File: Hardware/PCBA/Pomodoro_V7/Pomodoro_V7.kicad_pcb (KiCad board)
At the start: 2 copper layers, 76 x 76 mm, 69 parts, among them IC1 ESP32-S2-MINI-2-N4, J1 Conn_01x02_Socket, J2 Conn_01x01_Pin, J3 Conn_01x01_Pin, J4 USB4120-03-C_REVA

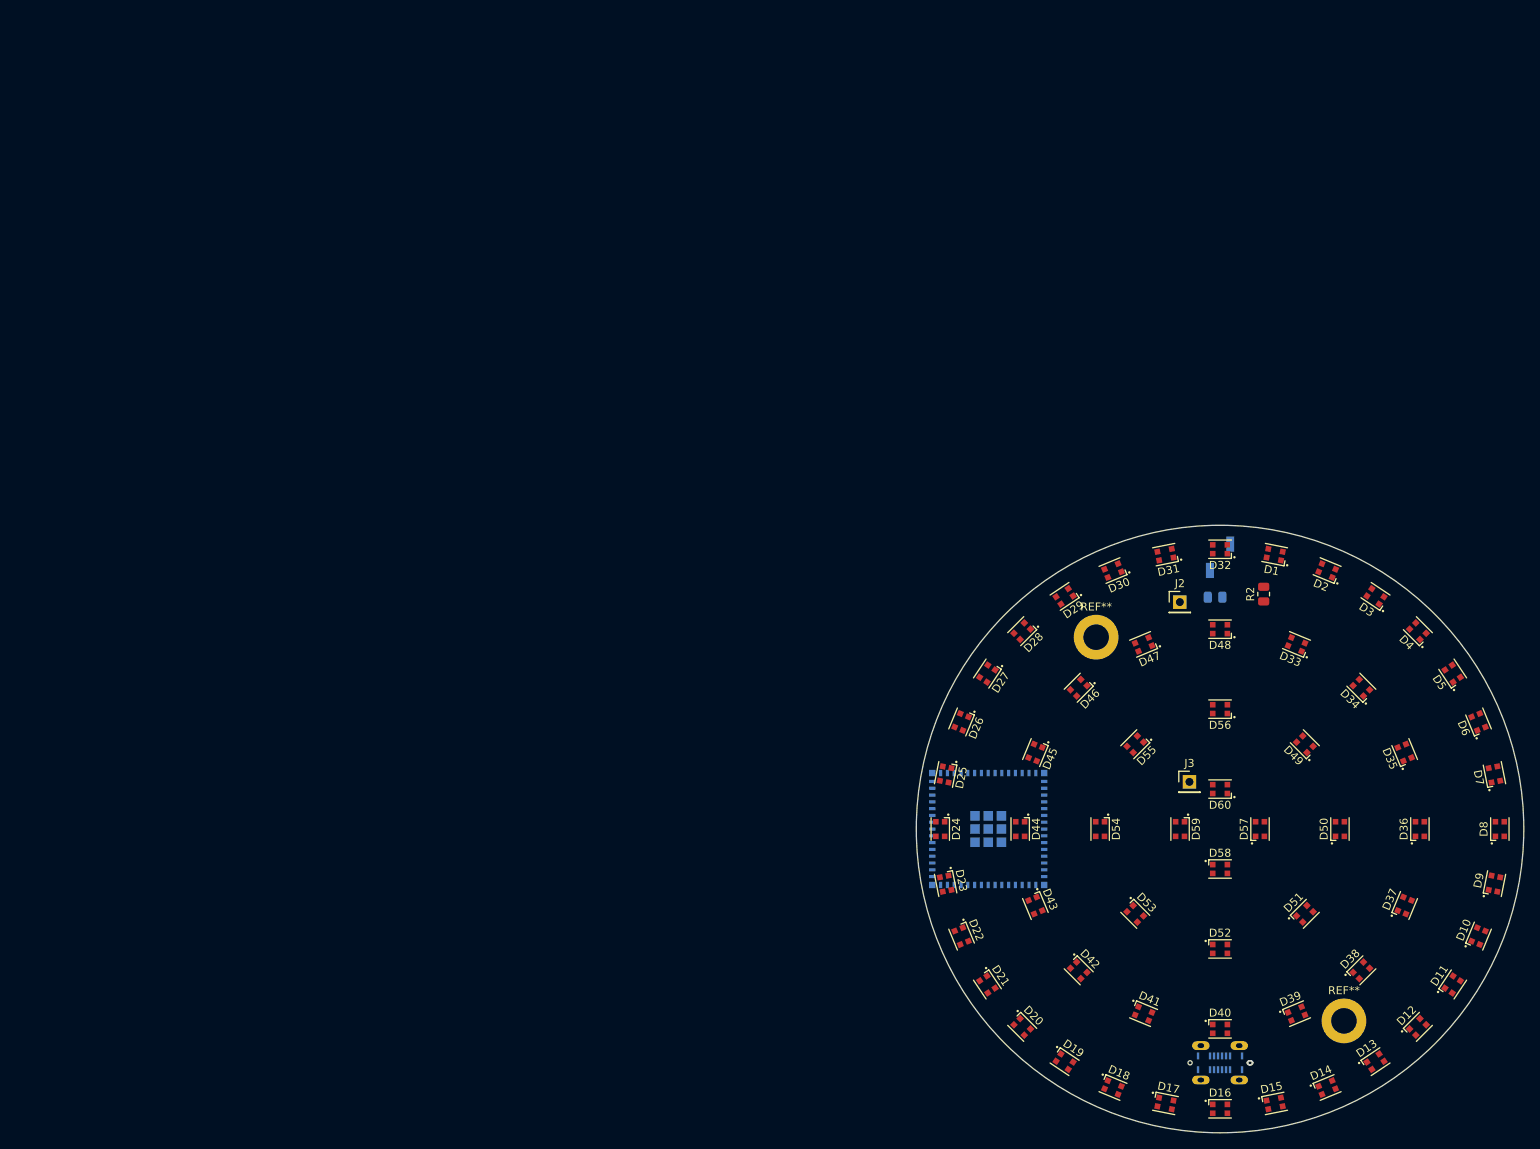
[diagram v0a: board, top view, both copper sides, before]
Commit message: FW can now be flashed to an ESP32-S2 Target; Completed the Schematic
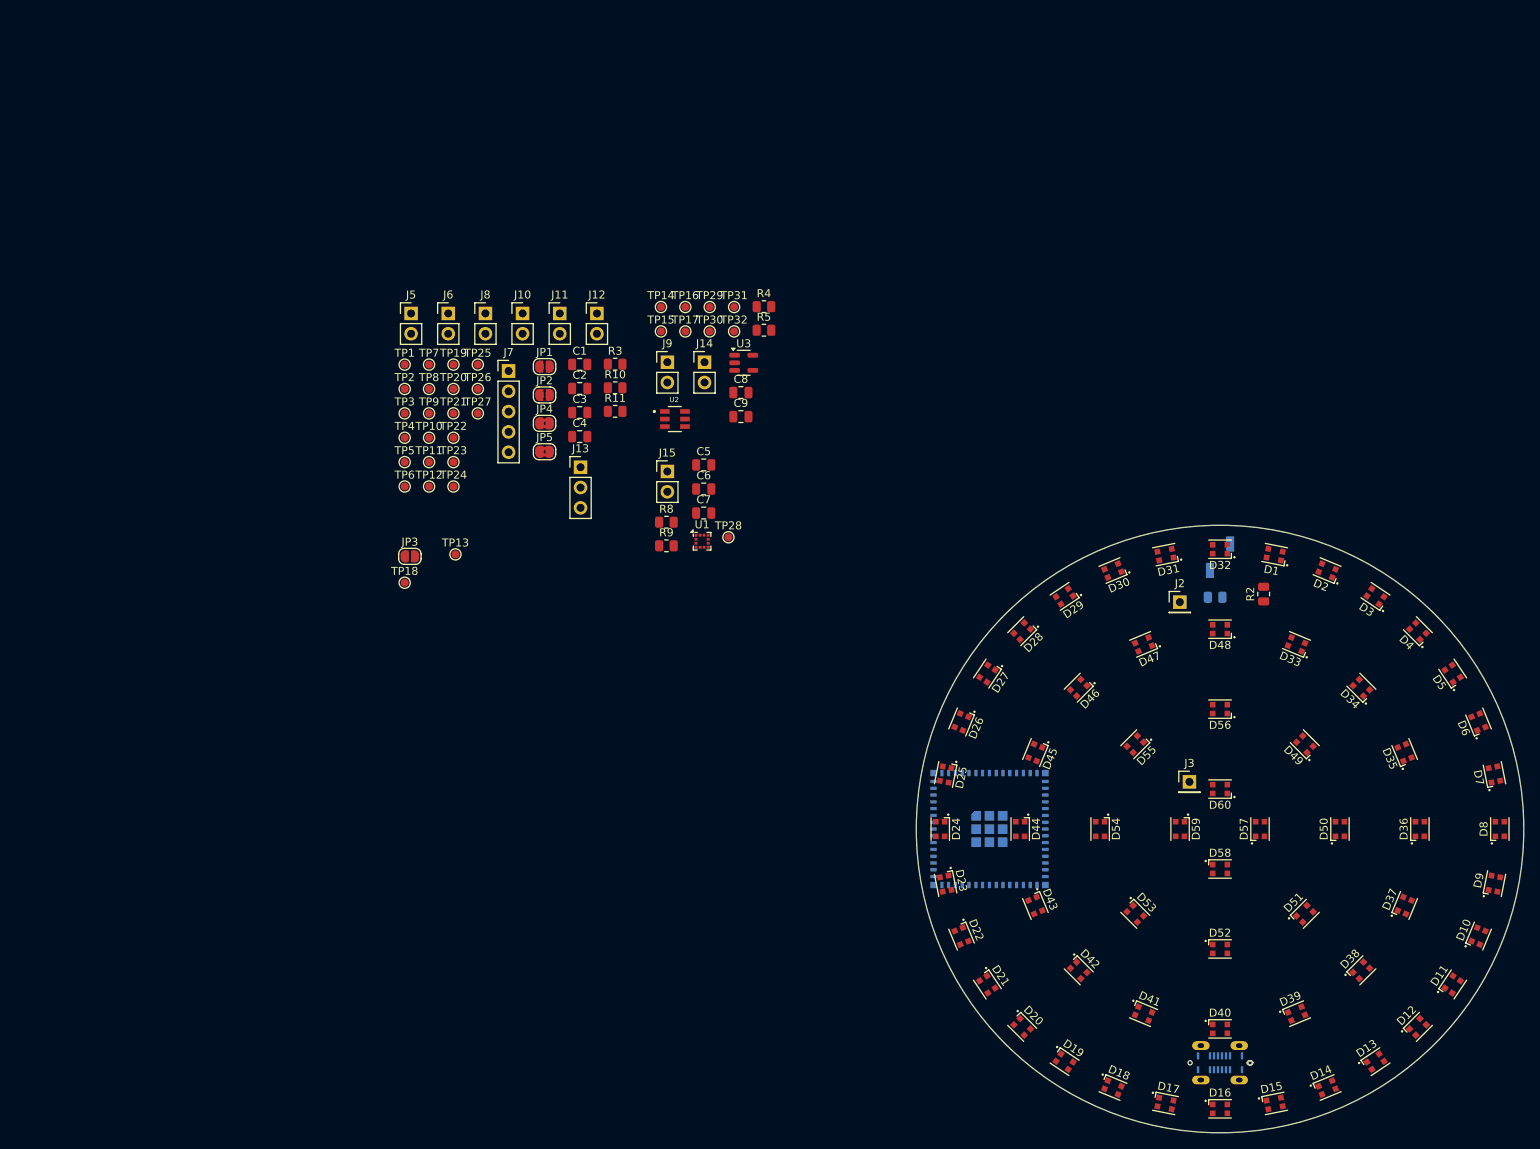
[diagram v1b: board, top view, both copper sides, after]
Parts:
- removed REF** (x2): MountingHole_3.2mm_M3_DIN965_Pad, MountingHole:MountingHole_3.2mm_M3_DIN965_Pad
- added C1: 10u/16V, Capacitor_SMD:C_0805_2012Metric, F.Cu at (69.9, 41.9)
- added C2: 10u/16V, Capacitor_SMD:C_0805_2012Metric, F.Cu at (69.9, 44.9)
- added C3: 100n/16V, Capacitor_SMD:C_0805_2012Metric, F.Cu at (69.9, 47.9)
- added C4: 1u/16V, Capacitor_SMD:C_0805_2012Metric, F.Cu at (69.9, 50.9)
- added C5: 1u/16V, Capacitor_SMD:C_0805_2012Metric, F.Cu at (85.4, 54.5)
- added C6: 100n/16V, Capacitor_SMD:C_0805_2012Metric, F.Cu at (85.4, 57.5)
- added C7: 100n/16V, Capacitor_SMD:C_0805_2012Metric, F.Cu at (85.4, 60.5)
- added C8: 1u/16V, Capacitor_SMD:C_0805_2012Metric, F.Cu at (90.1, 45.4)
- added C9: 1u/16V, Capacitor_SMD:C_0805_2012Metric, F.Cu at (90.1, 48.4)
- added J10: Conn_01x02_Pin, Connector_PinHeader_2.54mm:PinHeader_1x02_P2.54mm_Vertical, F.Cu at (62.8, 35.5)
- added J11: Conn_01x02_Pin, Connector_PinHeader_2.54mm:PinHeader_1x02_P2.54mm_Vertical, F.Cu at (67.4, 35.5)
- added J12: Conn_01x02_Pin, Connector_PinHeader_2.54mm:PinHeader_1x02_P2.54mm_Vertical, F.Cu at (72.0, 35.5)
- added J13: Conn_01x03_Pin, Connector_PinHeader_2.54mm:PinHeader_1x03_P2.54mm_Vertical, F.Cu at (70.0, 54.7)
- added J14: Conn_01x02_Pin, Connector_PinHeader_2.54mm:PinHeader_1x02_P2.54mm_Vertical, F.Cu at (85.5, 41.6)
- added J15: Conn_01x02_Pin, Connector_PinHeader_2.54mm:PinHeader_1x02_P2.54mm_Vertical, F.Cu at (80.9, 55.3)
- added J5: Conn_01x02_Pin, Connector_PinHeader_2.54mm:PinHeader_1x02_P2.54mm_Vertical, F.Cu at (48.8, 35.5)
- added J6: Conn_01x02_Pin, Connector_PinHeader_2.54mm:PinHeader_1x02_P2.54mm_Vertical, F.Cu at (53.5, 35.5)
- added J7: Conn_01x05_Pin, Connector_PinHeader_2.54mm:PinHeader_1x05_P2.54mm_Vertical, F.Cu at (61.0, 42.7)
- added J8: Conn_01x02_Pin, Connector_PinHeader_2.54mm:PinHeader_1x02_P2.54mm_Vertical, F.Cu at (58.1, 35.5)
- added J9: Conn_01x02_Pin, Connector_PinHeader_2.54mm:PinHeader_1x02_P2.54mm_Vertical, F.Cu at (80.9, 41.6)
- added JP1: SolderJumper_2_Open, Jumper:SolderJumper-2_P1.3mm_Open_RoundedPad1.0x1.5mm, F.Cu at (65.5, 42.1)
- added JP2: SolderJumper_2_Open, Jumper:SolderJumper-2_P1.3mm_Open_RoundedPad1.0x1.5mm, F.Cu at (65.5, 45.7)
- added JP3: SolderJumper_2_Open, Jumper:SolderJumper-2_P1.3mm_Open_RoundedPad1.0x1.5mm, F.Cu at (48.6, 65.9)
- added JP4: SolderJumper_2_Bridged, Jumper:SolderJumper-2_P1.3mm_Bridged2Bar_RoundedPad1.0x1.5mm, F.Cu at (65.5, 49.2)
- added JP5: SolderJumper_2_Bridged, Jumper:SolderJumper-2_P1.3mm_Bridged2Bar_RoundedPad1.0x1.5mm, F.Cu at (65.5, 52.8)
- added R10: 5k1, Resistor_SMD:R_0805_2012Metric, F.Cu at (74.3, 44.8)
- added R11: 5k1, Resistor_SMD:R_0805_2012Metric, F.Cu at (74.3, 47.8)
- added R3: 10k, Resistor_SMD:R_0805_2012Metric, F.Cu at (74.3, 41.9)
- added R4: 5k1, Resistor_SMD:R_0805_2012Metric, F.Cu at (92.9, 34.6)
- added R5: 5k1, Resistor_SMD:R_0805_2012Metric, F.Cu at (92.9, 37.6)
- added R8: 5k1, Resistor_SMD:R_0805_2012Metric, F.Cu at (80.7, 61.6)
- added R9: 5k1, Resistor_SMD:R_0805_2012Metric, F.Cu at (80.7, 64.6)
- added TP1: TestPoint, TestPoint:TestPoint_Pad_D1.0mm, F.Cu at (48.0, 41.9)
- added TP10: TestPoint, TestPoint:TestPoint_Pad_D1.0mm, F.Cu at (51.0, 51.0)
- added TP11: TestPoint, TestPoint:TestPoint_Pad_D1.0mm, F.Cu at (51.0, 54.1)
- added TP12: TestPoint, TestPoint:TestPoint_Pad_D1.0mm, F.Cu at (51.0, 57.1)
- added TP13: TestPoint, TestPoint:TestPoint_Pad_D1.0mm, F.Cu at (54.4, 65.6)
- added TP14: TestPoint, TestPoint:TestPoint_Pad_D1.0mm, F.Cu at (80.1, 34.7)
- added TP15: TestPoint, TestPoint:TestPoint_Pad_D1.0mm, F.Cu at (80.1, 37.8)
- added TP16: TestPoint, TestPoint:TestPoint_Pad_D1.0mm, F.Cu at (83.1, 34.7)
- added TP17: TestPoint, TestPoint:TestPoint_Pad_D1.0mm, F.Cu at (83.1, 37.8)
- added TP18: TestPoint, TestPoint:TestPoint_Pad_D1.0mm, F.Cu at (48.0, 69.2)
- added TP19: TestPoint, TestPoint:TestPoint_Pad_D1.0mm, F.Cu at (54.1, 41.9)
- added TP2: TestPoint, TestPoint:TestPoint_Pad_D1.0mm, F.Cu at (48.0, 45.0)
- added TP20: TestPoint, TestPoint:TestPoint_Pad_D1.0mm, F.Cu at (54.1, 45.0)
- added TP21: TestPoint, TestPoint:TestPoint_Pad_D1.0mm, F.Cu at (54.1, 48.0)
- added TP22: TestPoint, TestPoint:TestPoint_Pad_D1.0mm, F.Cu at (54.1, 51.0)
- added TP23: TestPoint, TestPoint:TestPoint_Pad_D1.0mm, F.Cu at (54.1, 54.1)
- added TP24: TestPoint, TestPoint:TestPoint_Pad_D1.0mm, F.Cu at (54.1, 57.1)
- added TP25: TestPoint, TestPoint:TestPoint_Pad_D1.0mm, F.Cu at (57.1, 41.9)
- added TP26: TestPoint, TestPoint:TestPoint_Pad_D1.0mm, F.Cu at (57.1, 45.0)
- added TP27: TestPoint, TestPoint:TestPoint_Pad_D1.0mm, F.Cu at (57.1, 48.0)
- added TP28: TestPoint, TestPoint:TestPoint_Pad_D1.0mm, F.Cu at (88.5, 63.5)
- added TP29: TestPoint, TestPoint:TestPoint_Pad_D1.0mm, F.Cu at (86.2, 34.7)
- added TP3: TestPoint, TestPoint:TestPoint_Pad_D1.0mm, F.Cu at (48.0, 48.0)
- added TP30: TestPoint, TestPoint:TestPoint_Pad_D1.0mm, F.Cu at (86.2, 37.8)
- added TP31: TestPoint, TestPoint:TestPoint_Pad_D1.0mm, F.Cu at (89.2, 34.7)
- added TP32: TestPoint, TestPoint:TestPoint_Pad_D1.0mm, F.Cu at (89.2, 37.8)
- added TP4: TestPoint, TestPoint:TestPoint_Pad_D1.0mm, F.Cu at (48.0, 51.0)
- added TP5: TestPoint, TestPoint:TestPoint_Pad_D1.0mm, F.Cu at (48.0, 54.1)
- added TP6: TestPoint, TestPoint:TestPoint_Pad_D1.0mm, F.Cu at (48.0, 57.1)
- added TP7: TestPoint, TestPoint:TestPoint_Pad_D1.0mm, F.Cu at (51.0, 41.9)
- added TP8: TestPoint, TestPoint:TestPoint_Pad_D1.0mm, F.Cu at (51.0, 45.0)
- added TP9: TestPoint, TestPoint:TestPoint_Pad_D1.0mm, F.Cu at (51.0, 48.0)
- added U1: LIS2HH12, Package_LGA:LGA-12_2x2mm_P0.5mm, F.Cu at (85.2, 64.0)
- added U2: USBLC6-2SC6, Diode_SMD:SOT95P280X145-6N, F.Cu at (81.8, 48.7)
- added U3: AP2112K-3.3, Package_TO_SOT_SMD:SOT-23-5, F.Cu at (90.4, 41.7)
- IC1: footprint RF_Module:ESP32S2MINI2N4 -> RF_Module:ESP32-S2-MINI-1
- R1: value 1k -> 10k
- moved IC1 2.40 mm to (118.6, 100.0)
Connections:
- net RgbLed_Dout renamed Net-(D60-DOUT)
- D47 pad 1: unconnected-(D47-DOUT-Pad1) -> Net-(D47-DOUT)
- D48 pad 3: unconnected-(D48-DIN-Pad3) -> Net-(D47-DOUT)
- IC1 pad 12: unconnected-(IC1-IO8-Pad12) -> /MicroController/ESP32_ALT_I2C_SDA
- IC1 pad 13: unconnected-(IC1-IO9-Pad13) -> /MicroController/ESP32_ALT_I2C_SCL
- IC1 pad 14: unconnected-(IC1-IO10-Pad14) -> /MicroController/ESP32_DBG3
- IC1 pad 15: unconnected-(IC1-IO11-Pad15) -> /MicroController/ESP32_DBG4
- IC1 pad 16: unconnected-(IC1-IO12-Pad16) -> ESP32_RgbLed_DOUT
- IC1 pad 17: unconnected-(IC1-IO13-Pad17) -> ESP32_RgbLed_DIN
- IC1 pad 18: unconnected-(IC1-IO14-Pad18) -> ESP32_Button_Signal
- IC1 pad 19: unconnected-(IC1-IO15-Pad19) -> IMU_INT1
- IC1 pad 20: unconnected-(IC1-IO16-Pad20) -> IMU_INT2
- IC1 pad 21: unconnected-(IC1-IO17-Pad21) -> /MicroController/ESP32_DBG5
- IC1 pad 22: unconnected-(IC1-IO18-Pad22) -> /MicroController/ESP32_DBG6
- IC1 pad 23: unconnected-(IC1-IO19-Pad23) -> ESP32_USB_D-
- IC1 pad 24: unconnected-(IC1-IO20-Pad24) -> ESP32_USB_D+
- IC1 pad 28: unconnected-(IC1-IO33-Pad28) -> /MicroController/ESP32_NOM_I2C_SDA
- IC1 pad 3: unconnected-(IC1-3V3-Pad3) -> +3V3
- IC1 pad 31: unconnected-(IC1-IO35-Pad31) -> /MicroController/ESP32_NOM_I2C_SCL
- IC1 pad 35: unconnected-(IC1-IO39-Pad35) -> /MicroController/JTAG_TCK
- IC1 pad 36: unconnected-(IC1-IO40-Pad36) -> /MicroController/JTAG_TDO
- IC1 pad 37: unconnected-(IC1-IO41-Pad37) -> /MicroController/JTAG_TDI
- IC1 pad 38: unconnected-(IC1-IO42-Pad38) -> /MicroController/JTAG_TMS
- IC1 pad 39: unconnected-(IC1-TXD0-Pad39) -> TXD0
- IC1 pad 4: unconnected-(IC1-IO0-Pad4) -> /MicroController/BOOT_OPTION
- IC1 pad 40: unconnected-(IC1-RXD0-Pad40) -> RXD0
- IC1 pad 45: unconnected-(IC1-EN-Pad45) -> /MicroController/ESP32_EN
- IC1 pad 7: unconnected-(IC1-IO3-Pad7) -> /MicroController/ESP32_DBG1
- IC1 pad 8: unconnected-(IC1-IO4-Pad8) -> /MicroController/ESP32_DBG2
- J1 pad 1: Button_Signal -> ESP32_Button_Signal
- J2 pad 1: RgbLed_PWM -> ESP32_RgbLed_DIN
- J4 pad A1: unconnected-(J4-GND_A-PadA1) -> GND
- J4 pad A12: unconnected-(J4-GND_A__1-PadA12) -> GND
- J4 pad A4: unconnected-(J4-VBUS_A-PadA4) -> VBUS
- J4 pad A5: unconnected-(J4-CC1-PadA5) -> Net-(J4-CC1)
- J4 pad A6: unconnected-(J4-D1+-PadA6) -> /USB Conn and PWR /CONN_USB_D_P
- J4 pad A7: unconnected-(J4-D1--PadA7) -> /USB Conn and PWR /CONN_USB_D_M
- J4 pad A9: unconnected-(J4-VBUS_A__1-PadA9) -> VBUS
- J4 pad B1: unconnected-(J4-GND_B-PadB1) -> GND
- J4 pad B12: unconnected-(J4-GND_B__1-PadB12) -> GND
- J4 pad B4: unconnected-(J4-VBUS_B-PadB4) -> VBUS
- J4 pad B5: unconnected-(J4-CC2-PadB5) -> Net-(J4-CC2)
- J4 pad B6: unconnected-(J4-D2+-PadB6) -> /USB Conn and PWR /CONN_USB_D_P
- J4 pad B7: unconnected-(J4-D2--PadB7) -> /USB Conn and PWR /CONN_USB_D_M
- J4 pad B9: unconnected-(J4-VBUS_B__1-PadB9) -> VBUS
- J4 pad S1: unconnected-(J4-SHIELD-PadS1) -> GND
- J4 pad S2: unconnected-(J4-SHIELD__1-PadS2) -> GND
- J4 pad S3: unconnected-(J4-SHIELD__2-PadS3) -> GND
- J4 pad S4: unconnected-(J4-SHIELD__3-PadS4) -> GND
- R1 pad 1: Button_Signal -> ESP32_Button_Signal
- R1 pad 2: +3.3V -> +3V3
- R2 pad 1: RgbLed_PWM -> ESP32_RgbLed_DIN

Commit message: added the selector wheel, changed the Connectors on the Trigger Button to move the assemlby closer together
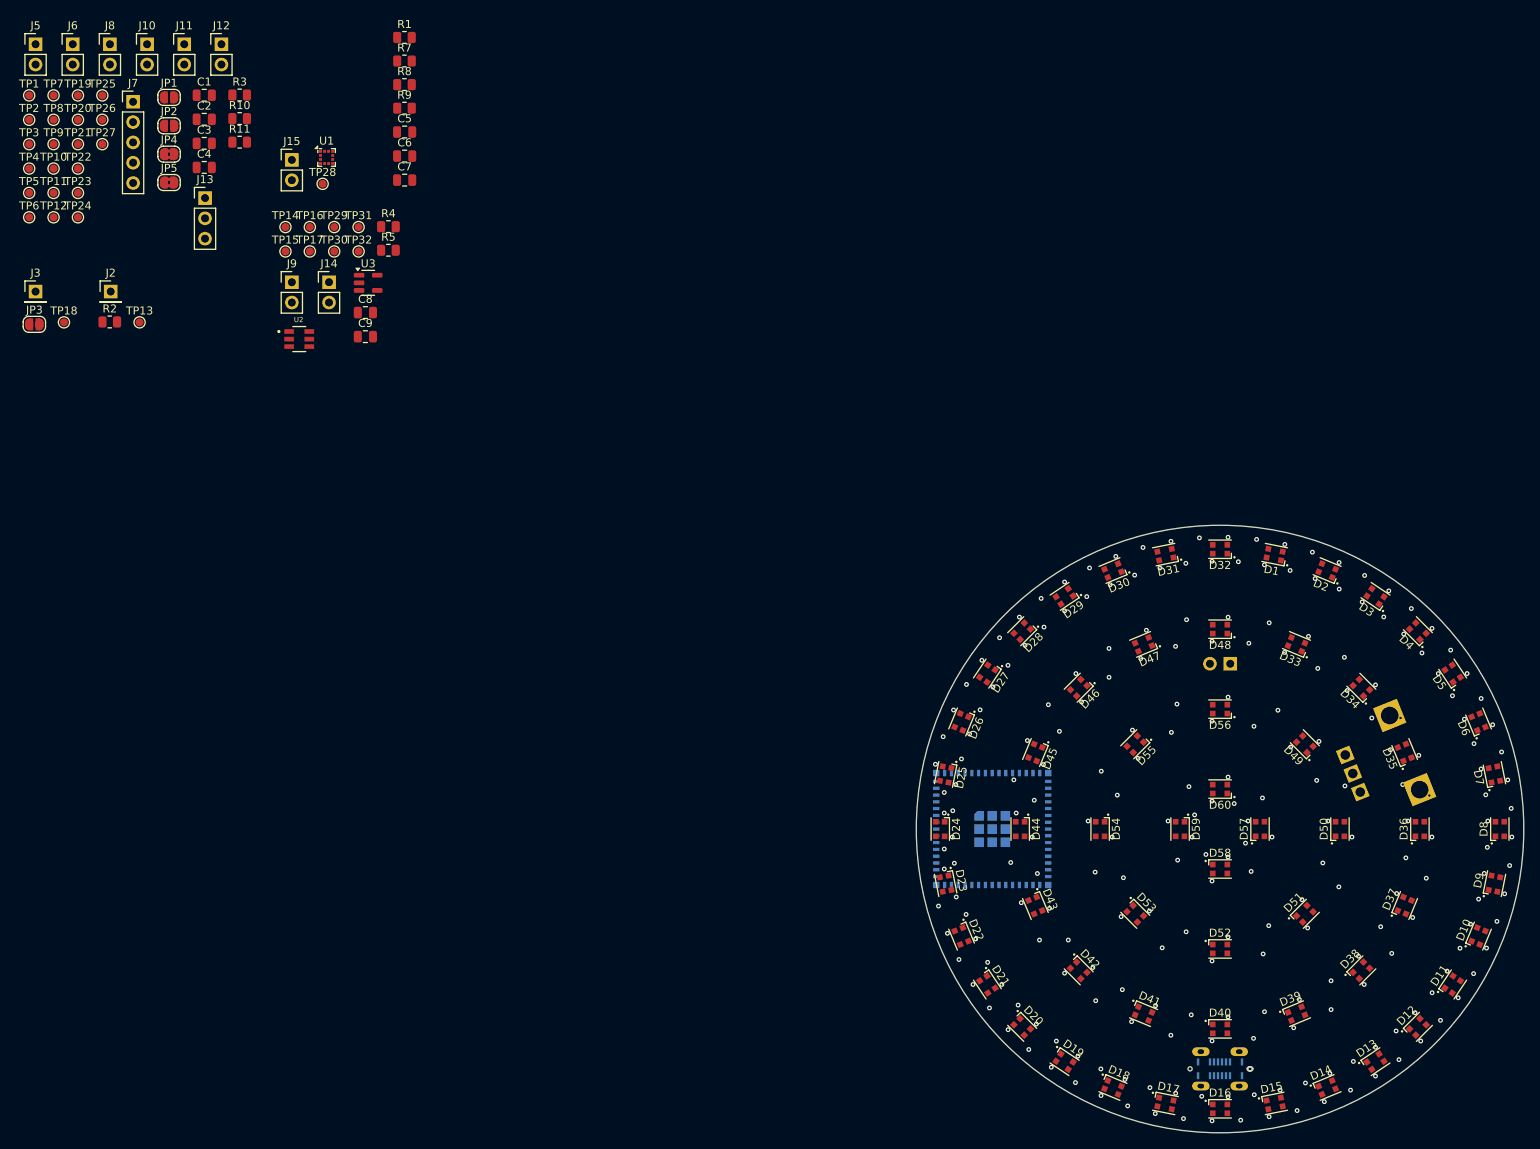
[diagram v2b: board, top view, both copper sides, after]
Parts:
- added R6: 2k 1/20W, Potentiometer_THT:Pot, B.Cu at (173.1, 90.4)
- added R7: 1k(1%), Resistor_SMD:R_0805_2012Metric, F.Cu at (48.0, 3.92)
- J1: value Conn_01x02_Socket -> Conn_01x02_Pin; footprint Connector_PinSocket_2.54mm:PinSocket_1x02_P2.54mm_Vertical_SMD_Pin1Right -> Connector_PinHeader_2.54mm:PinHeader_1x02_P2.54mm_Horizontal
- R1: value 10k -> 10k(1%); moved to F.Cu
- R10, R11, R4, R5, R8, R9: value 5k1 -> 5k1(1%)
- R3: value 10k -> 10k(1%)
- moved J3 156.8 mm to (1.82, 32.8)
- moved R2 148.3 mm to (11.1, 36.6), turned to 0 degrees
- moved J2 139.3 mm to (11.2, 32.8)
- moved R1 123.2 mm to (48.0, 0.97), turned to 0 degrees
- moved TP28 67.3 mm to (37.7, 19.3)
- moved U1 67.2 mm to (38.2, 16.0)
- moved R9 63.8 mm to (48.0, 9.82)
- moved R8 63.8 mm to (48.0, 6.88)
- moved J15 61.0 mm to (33.9, 16.3)
- moved J7 57.8 mm to (14.0, 9.03)
- moved JP2 57.8 mm to (18.5, 12.0)
- moved TP2 57.8 mm to (1.02, 11.3)
- moved TP20 57.8 mm to (7.12, 11.3)
- moved C1 57.8 mm to (22.9, 8.21)
- moved C2 57.8 mm to (22.9, 11.2)
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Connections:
- C8 pad 1: VBUS -> +5V
- IC1 pad 5: unconnected-(IC1-IO1-Pad5) -> ESP32_ADC_POTI
- J1 pad 1: ESP32_Button_Signal -> GND
- J1 pad 2: GND -> ESP32_Button_Signal
- J4 pad A4: VBUS -> +5V
- J4 pad A9: VBUS -> +5V
- J4 pad B4: VBUS -> +5V
- J4 pad B9: VBUS -> +5V
- J9 pad 2: VBUS -> +5V
- R10 pad 1: +3V3 -> I2C_SCL
- R10 pad 2: I2C_SCL -> +3V3
- R11 pad 1: +3V3 -> I2C_SDA
- R11 pad 2: I2C_SDA -> +3V3
- R5 pad 1: Net-(J4-CC1) -> GND
- R5 pad 2: GND -> Net-(J4-CC1)
- TP14 pad 1: VBUS -> +5V
- TP15 pad 1: VBUS -> +5V
- U2 pad 5: VBUS -> +5V
- U3 pad 1: VBUS -> +5V
- U3 pad 3: VBUS -> +5V
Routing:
- net GND: vias 0 -> 120
- net +5V: vias 0 -> 120
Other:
- copper layers 2 -> 4
